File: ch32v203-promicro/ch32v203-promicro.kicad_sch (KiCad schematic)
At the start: 27 parts, among them J1 USB2.0_C_v3, J2 ProMicro-LeftPin, J3 ProMicro-RightPin, SW1 SW_Push, SW2 SW_Push, U1 CH32V203CxT6, U2 AMS1117-3.3, Y1 32.768k, Y2 8M

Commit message: stm32
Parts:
- added JP1: Jumper_3_Open, Jumper:SolderJumper-3_P1.3mm_Open_RoundedPad1.0x1.5mm, symbol Jumper:Jumper_3_Open
- added R8: 10k, $74th:Register_0805_2012, symbol Device:R
- J2: value ProMicro-LeftPin -> ProMicro-LeftPin-NoGND; footprint $74th:ProMicro_LIKE_LEFT -> $74th:ProMicro_LIKE_LEFT_NO_GND; symbol $74th:ProMicro-LeftPin -> $74th:ProMicro-LeftPin-NoGND
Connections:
- net +3V3: now also JP1.3 (B)
- net 10/A10: now also U1.14 (PA4/ADC4/SPI1_NSS/UART2_CK); no longer U1.38 (PA15)
- net GND: now also JP1.1 (A), R8.2; no longer J2.3 (GND), J2.4 (GND), SW1.1
- net RST: now also R8.1
- net SWDIO: now reaches U1.34 (SWDIO/PA13)
- net SWDIO: now also J2.3 (Alt1)
- net SWCLK: now reaches U1.37 (SWCLK/PA14)
- net SWCLK: now also J2.4 (Alt2)
- new net: JP1.2 (C), SW1.1
- no-connect marks 13 -> 11
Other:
- moved on the sheet: C6, J2, J3, R2, SW1

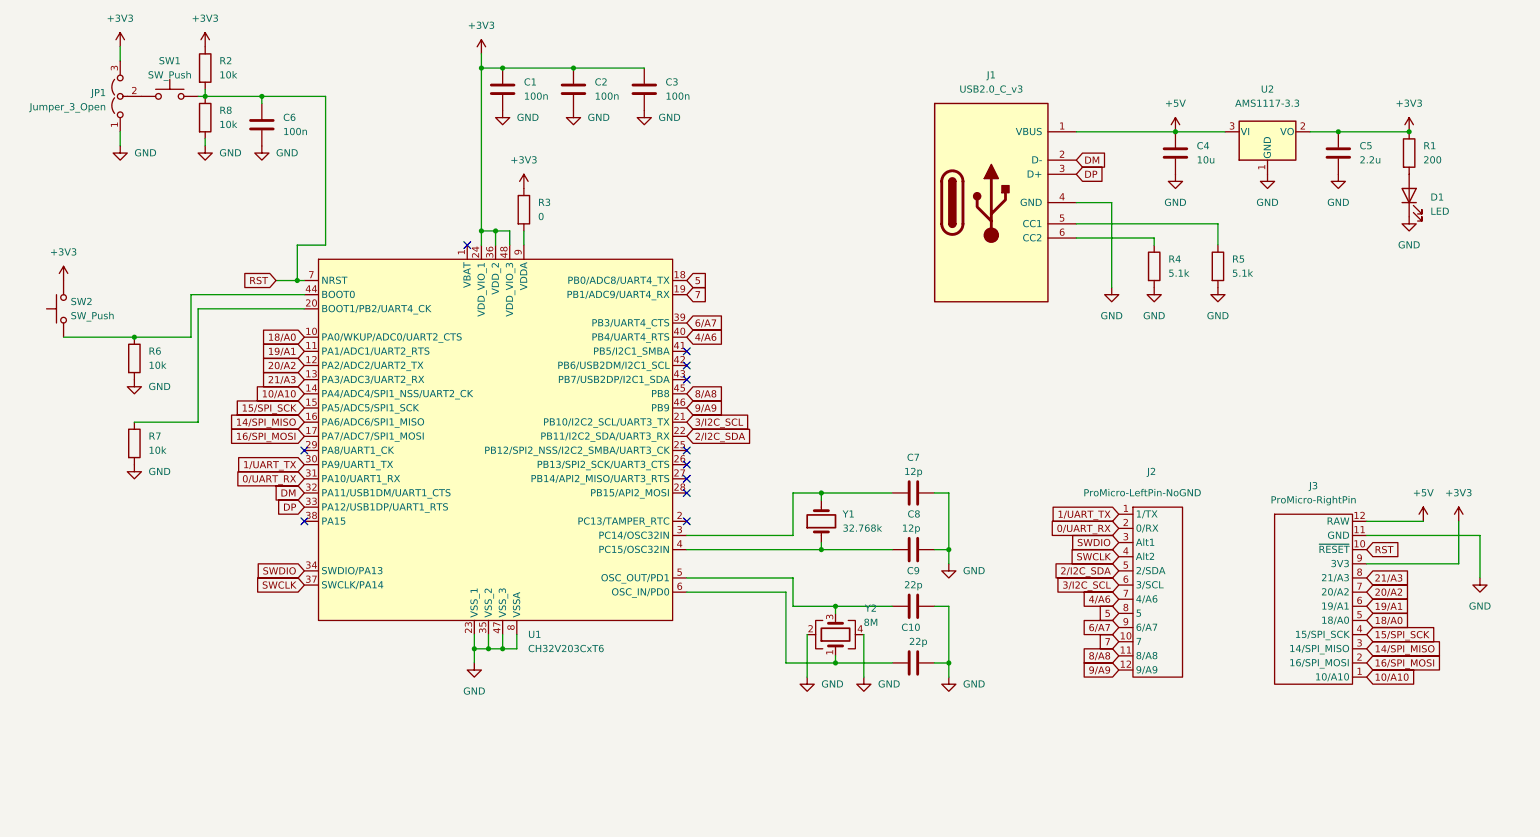
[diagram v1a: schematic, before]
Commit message: x32micro v1.1.0
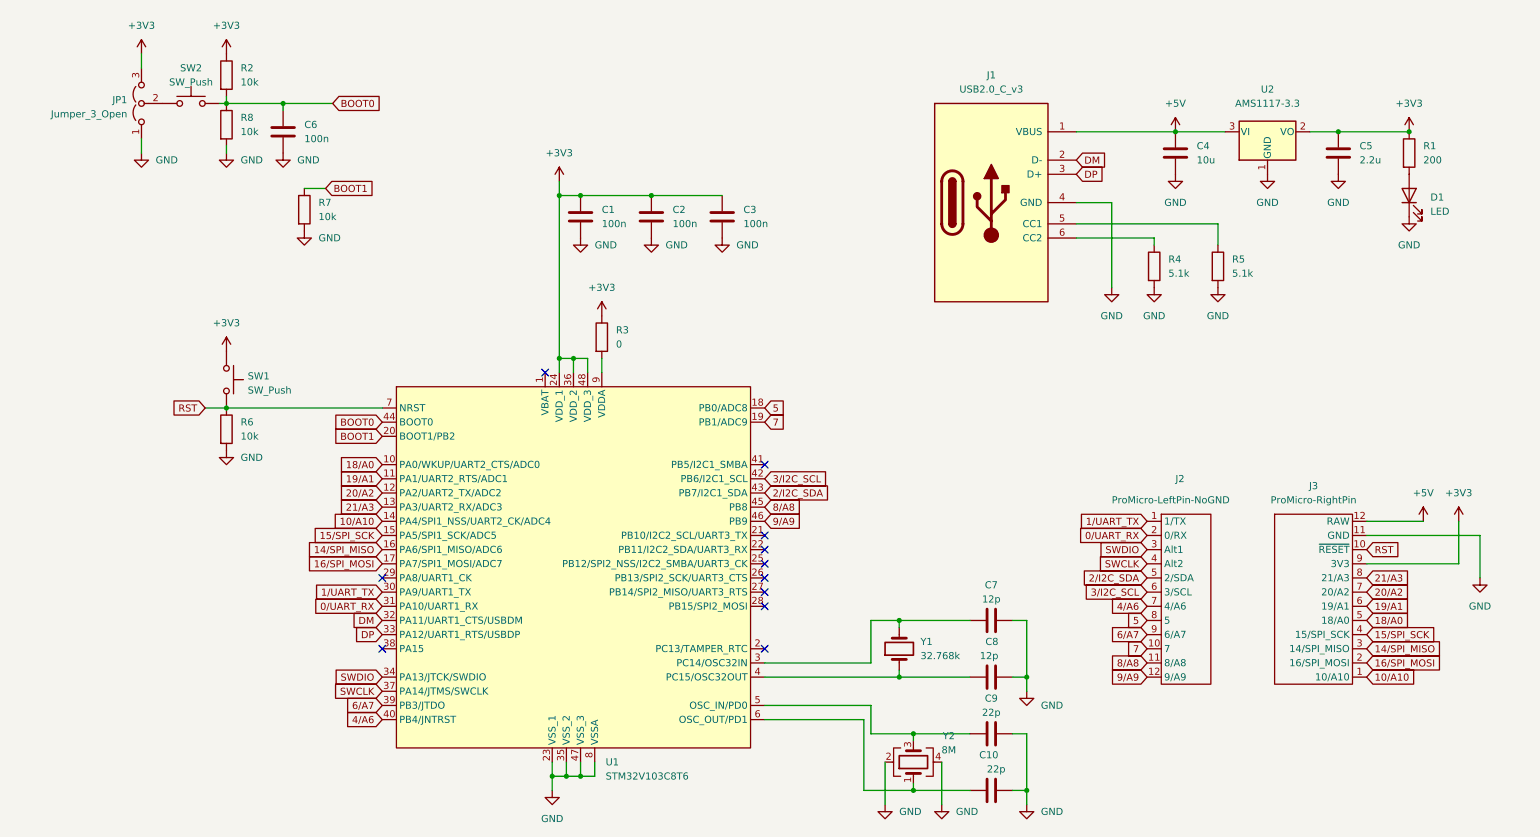
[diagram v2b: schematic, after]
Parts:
- removed U1: CH32V203CxT6, Package_QFP:LQFP-48_7x7mm_P0.5mm, symbol ch32v-dev-boards:CH32V203CxT6
- added U1: STM32V103C8T6, Package_QFP:LQFP-48_7x7mm_P0.5mm, symbol $74th:STM32F103C8T6
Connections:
- net +3V3: now also SW1.1, U1.24 (VDD_1), U1.36 (VDD_2), U1.48 (VDD_3); no longer SW2.2
- net 0/UART_RX: now also U1.31 (PA10/UART1_RX)
- net 10/A10: now also U1.14 (PA4/SPI1_NSS/UART2_CK/ADC4)
- net 14/SPI_MISO: now also U1.16 (PA6/SPI1_MISO/ADC6)
- net 15/SPI_SCK: now also U1.15 (PA5/SPI1_SCK/ADC5)
- net 16/SPI_MOSI: now also U1.17 (PA7/SPI1_MOSI/ADC7)
- net 18/A0: now also U1.10 (PA0/WKUP/UART2_CTS/ADC0)
- net 19/A1: now also U1.11 (PA1/UART2_RTS/ADC1)
- net 1/UART_TX: now also U1.30 (PA9/UART1_TX)
- net 20/A2: now also U1.12 (PA2/UART2_TX/ADC2)
- net 21/A3: now also U1.13 (PA3/UART2_RX/ADC3)
- net 2/I2C_SDA: now also U1.43 (PB7/I2C1_SDA)
- net 3/I2C_SCL: now also U1.42 (PB6/I2C1_SCL)
- net 4/A6: now also U1.40 (PB4/JNTRST)
- net 5: now also U1.18 (PB0/ADC8)
- net 6/A7: now also U1.39 (PB3/JTDO)
- net 7: now also U1.19 (PB1/ADC9)
- net 8/A8: now also U1.45 (PB8)
- net 9/A9: now also U1.46 (PB9)
- net DM: now also U1.32 (PA11/UART1_CTS/USBDM)
- net DP: now also U1.33 (PA12/UART1_RTS/USBDP)
- net GND: now also U1.23 (VSS_1), U1.35 (VSS_2), U1.47 (VSS_3), U1.8 (VSSA)
- net RST: now also R6.1, U1.7 (NRST); no longer C6.1, R2.2, R8.1
- net SWCLK: now also U1.37 (PA14/JTMS/SWCLK)
- net SWDIO: now also U1.34 (PA13/JTCK/SWDIO)
- net at R3.2: now also U1.9 (VDDA)
- net at SW2.1: now also JP1.2 (C); no longer R6.1
- net at C7.1, Y1.2: now also U1.3 (PC14/OSC32IN)
- net at C10.1, Y2.1: now also U1.6 (OSC_OUT/PD1)
- net BOOT1: now reaches R7.1
- net BOOT1: now also U1.20 (BOOT1/PB2)
- net at C9.1, Y2.3: now also U1.5 (OSC_IN/PD0)
- net at C8.1, Y1.1: now also U1.4 (PC15/OSC32OUT)
- new net BOOT0: C6.1, R2.2, R8.1, SW2.2, U1.44 (BOOT0)
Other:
- title: (none) -> STM32Micro
- moved on the sheet: C1, C10, C2, C3, C6, C7, C8, C9, J2, JP1, R2, R3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
